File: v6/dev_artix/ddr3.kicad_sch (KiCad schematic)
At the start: 20 parts, among them U501 AS4C256M16D3

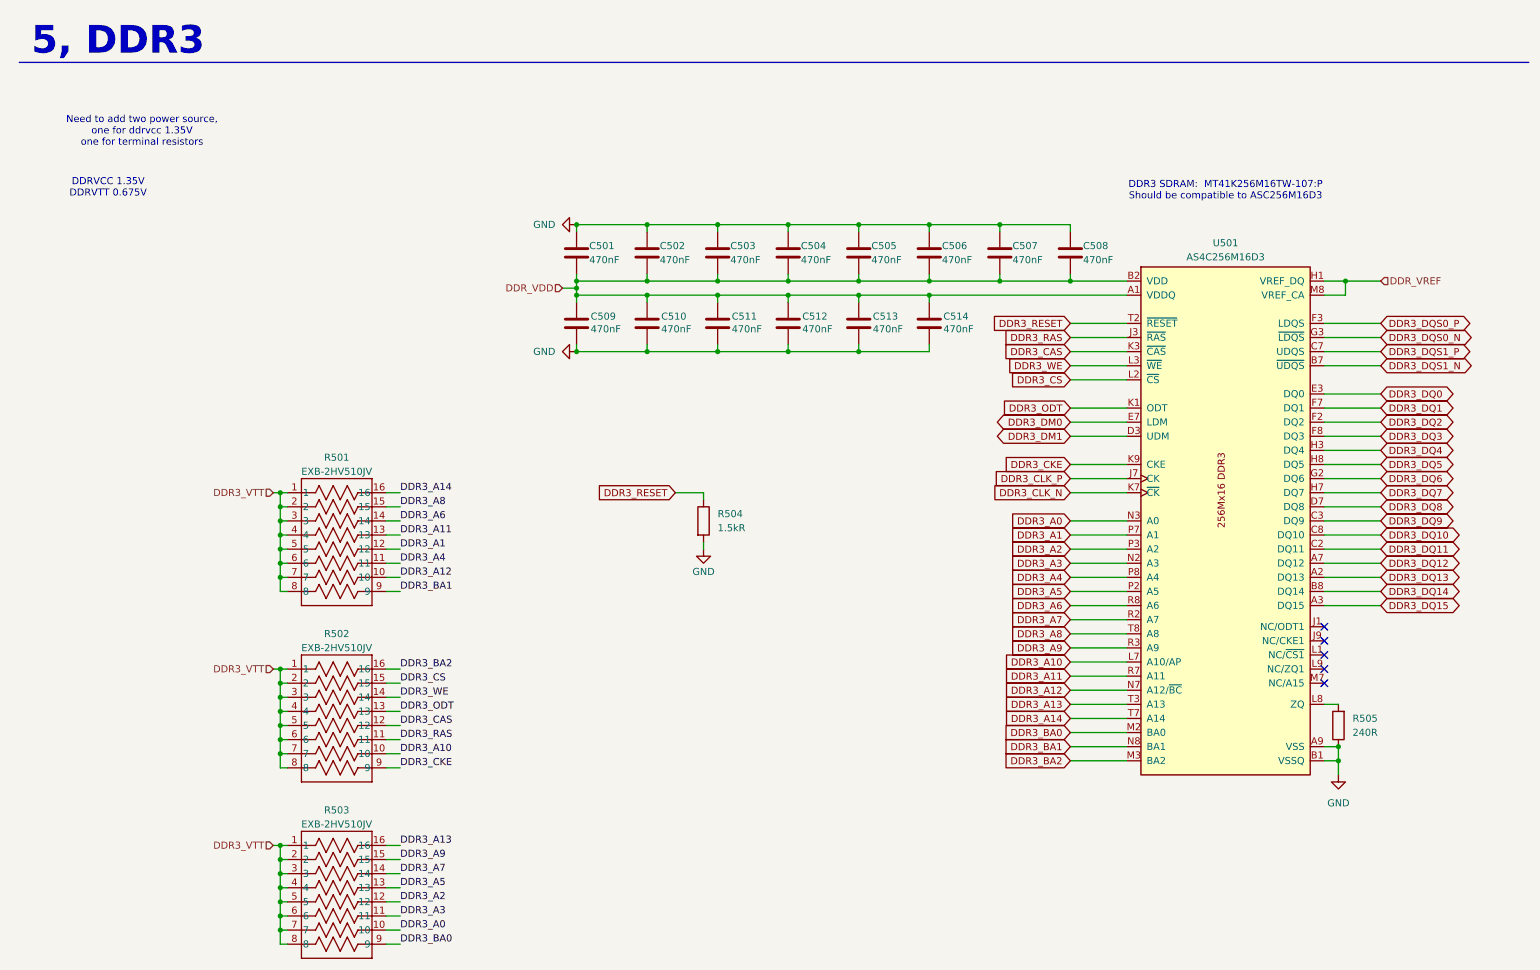
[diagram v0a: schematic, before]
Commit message: Adapt numbers for easier ordering and assembling
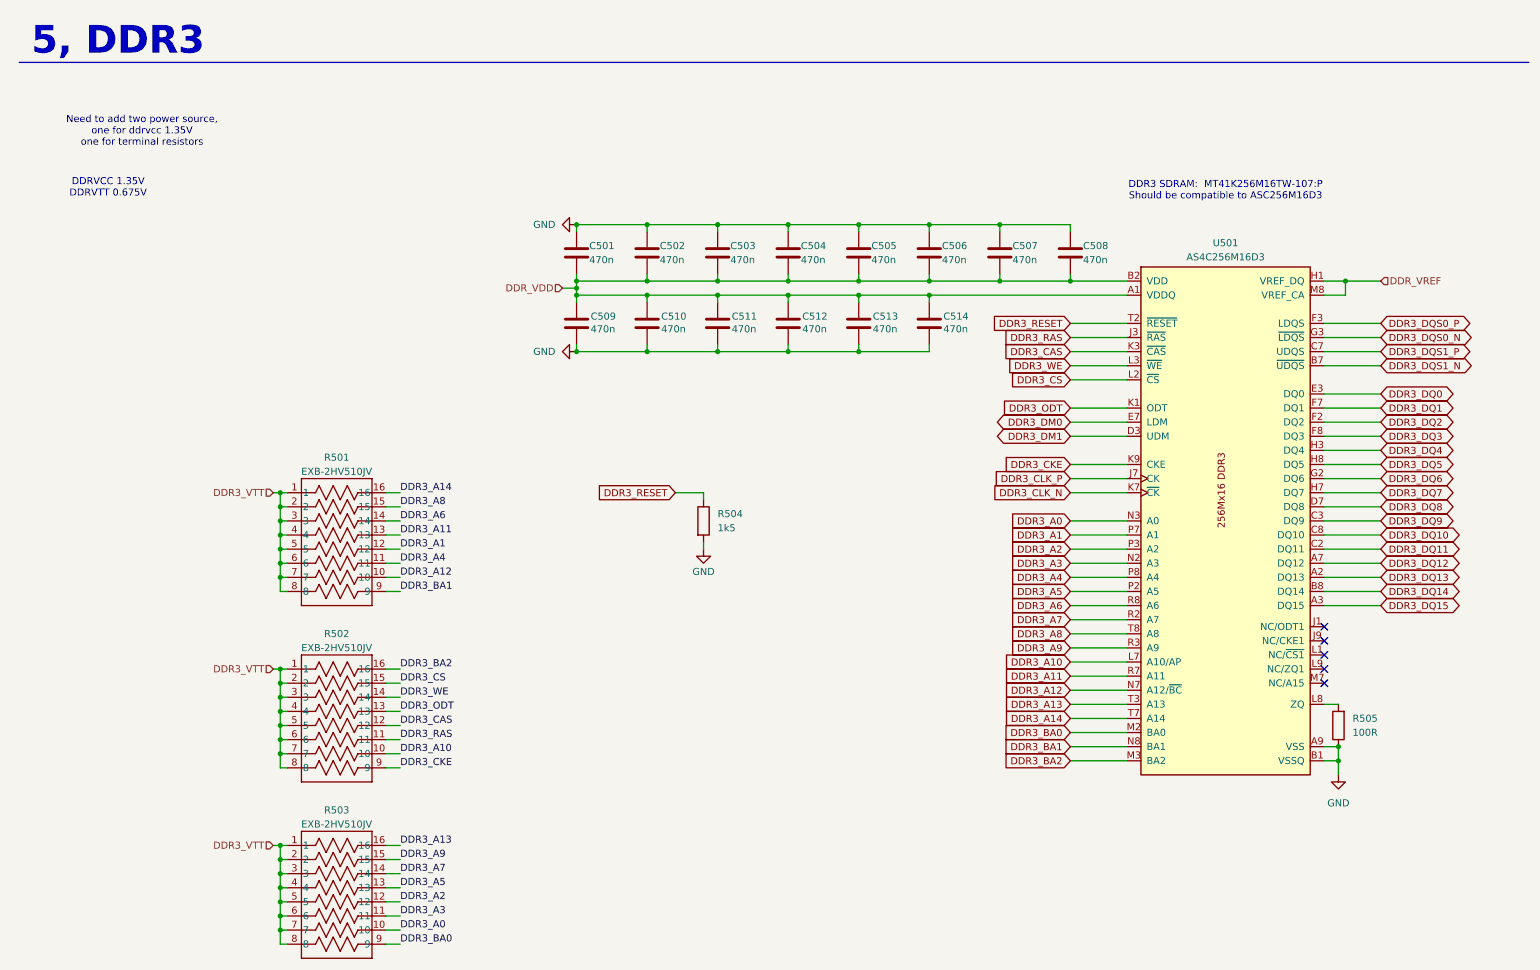
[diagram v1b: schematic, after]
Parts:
- C501, C502, C503, C504, C505, C506, C507, C508, C509, C510, C511, C512, C513, C514: value 470nF -> 470n
- R504: value 1.5kR -> 1k5
- R505: value 240R -> 100R
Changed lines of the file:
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@@
 			)
 		)
-		(property "Value" "470nF"
+		(property "Value" "470n"
 			(at 140.716 55.88 0)
 			(effects
@@
 			)
 		)
-		(property "Value" "470nF"
+		(property "Value" "470n"
 			(at 140.97 68.326 0)
 			(effects
@@
 			)
 		)
-		(property "Value" "470nF"
+		(property "Value" "470n"
 			(at 191.516 55.88 0)
 			(effects
@@
 			)
 		)
-		(property "Value" "240R"
+		(property "Value" "100R"
 			(at 252.73 140.9699 0)
 			(effects
@@
 			)
 		)
-		(property "Value" "470nF"
+		(property "Value" "470n"
 			(at 179.07 68.326 0)
 			(effects
@@
 			)
 		)
-		(property "Value" "470nF"
+		(property "Value" "470n"
 			(at 204.216 55.88 0)
 			(effects
@@
 			)
 		)
-		(property "Value" "470nF"
+		(property "Value" "470n"
 			(at 166.116 55.88 0)
 			(effects
@@
 			)
 		)
-		(property "Value" "470nF"
+		(property "Value" "470n"
 			(at 128.016 55.88 0)
 			(effects
@@
 			)
 		)
-		(property "Value" "470nF"
+		(property "Value" "470n"
 			(at 115.316 55.88 0)
 			(effects
@@
 			)
 		)
-		(property "Value" "470nF"
+		(property "Value" "470n"
 			(at 178.816 55.88 0)
 			(effects
@@
 			)
 		)
-		(property "Value" "470nF"
+		(property "Value" "470n"
 			(at 128.27 68.326 0)
 			(effects
@@
 			)
 		)
-		(property "Value" "470nF"
+		(property "Value" "470n"
 			(at 166.37 68.326 0)
 			(effects
@@
 			)
 		)
-		(property "Value" "470nF"
+		(property "Value" "470n"
 			(at 153.416 55.88 0)
 			(effects
@@
 			)
 		)
-		(property "Value" "470nF"
+		(property "Value" "470n"
 			(at 115.57 68.326 0)
 			(effects
@@
 			)
 		)
-		(property "Value" "470nF"
+		(property "Value" "470n"
 			(at 153.67 68.326 0)
 			(effects
@@
 			)
 		)
-		(property "Value" "1.5kR"
+		(property "Value" "1k5"
 			(at 138.43 104.1399 0)
 			(effects
